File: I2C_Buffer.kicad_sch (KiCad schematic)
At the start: 6 parts, among them U2 LTC4300A-1IMS8_PBF

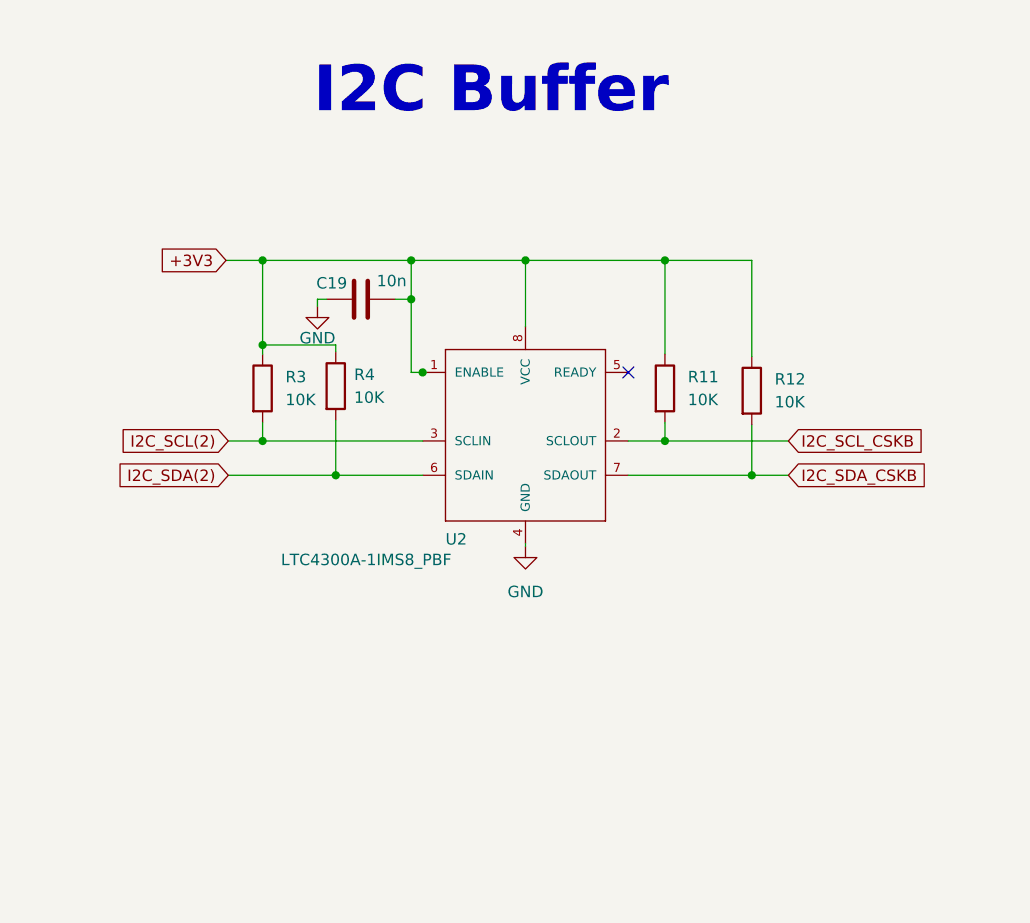
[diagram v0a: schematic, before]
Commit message: Fixed GND issues with connector and mounting holes
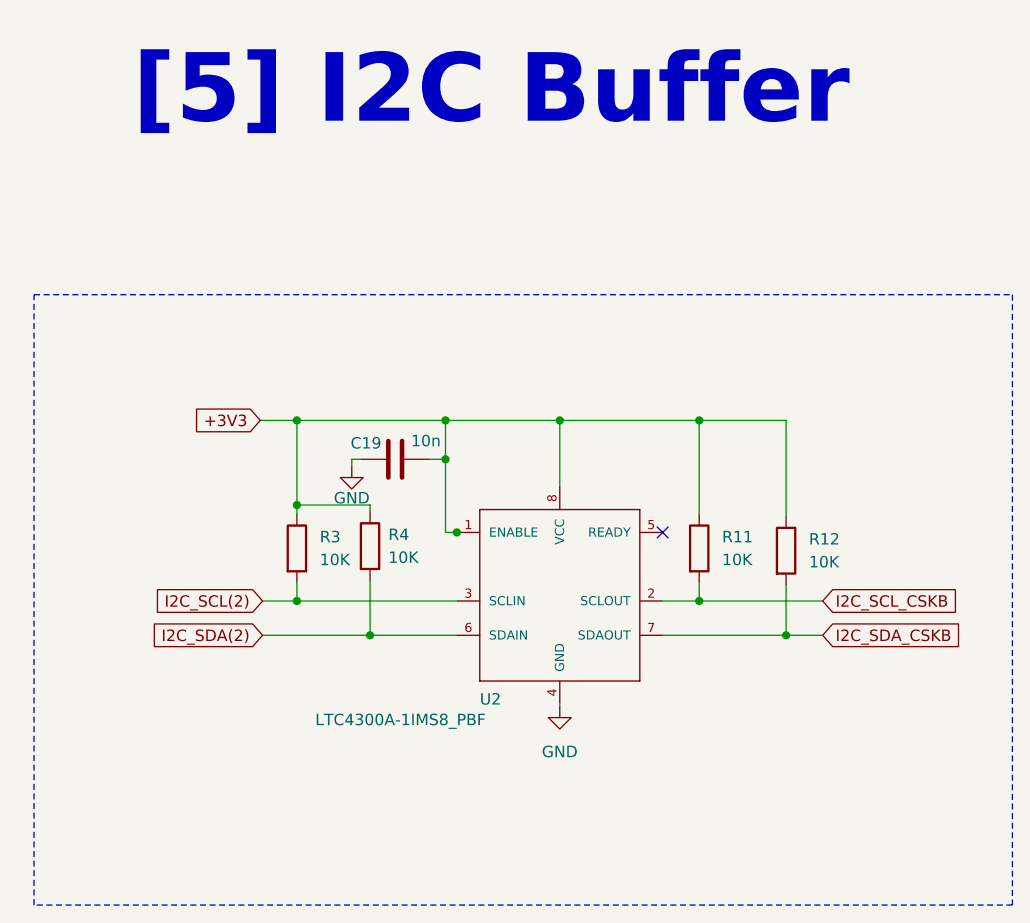
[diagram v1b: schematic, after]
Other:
- note added: "[5] I2C Buffer"
- note removed: "I2C Buffer"
- moved on the sheet: C19, R11, R12, R3, R4, U2
